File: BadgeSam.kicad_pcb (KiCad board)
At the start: 2 copper layers, 69.6 x 45 mm, 16 parts, among them J1 PROG, SW1 RESET, U1 STM8S003F3P

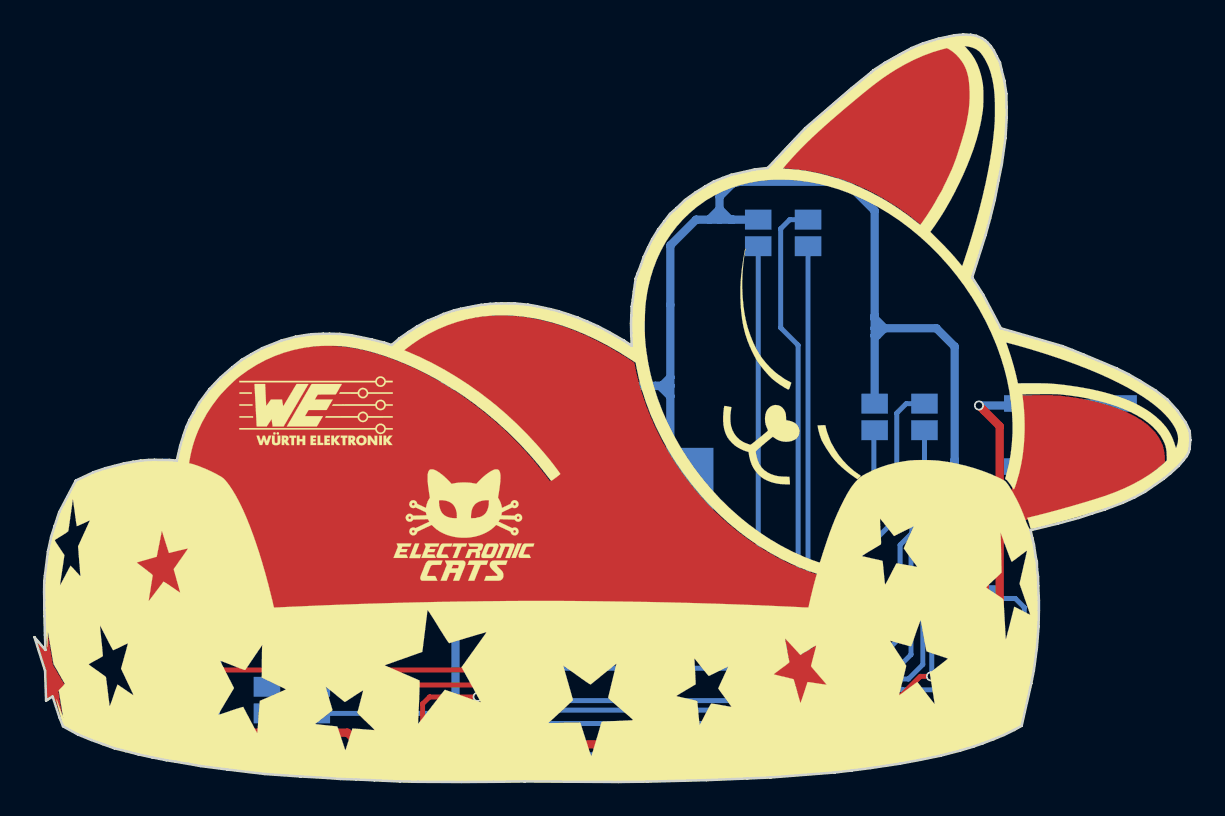
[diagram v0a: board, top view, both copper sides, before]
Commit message: Fix leds and traces
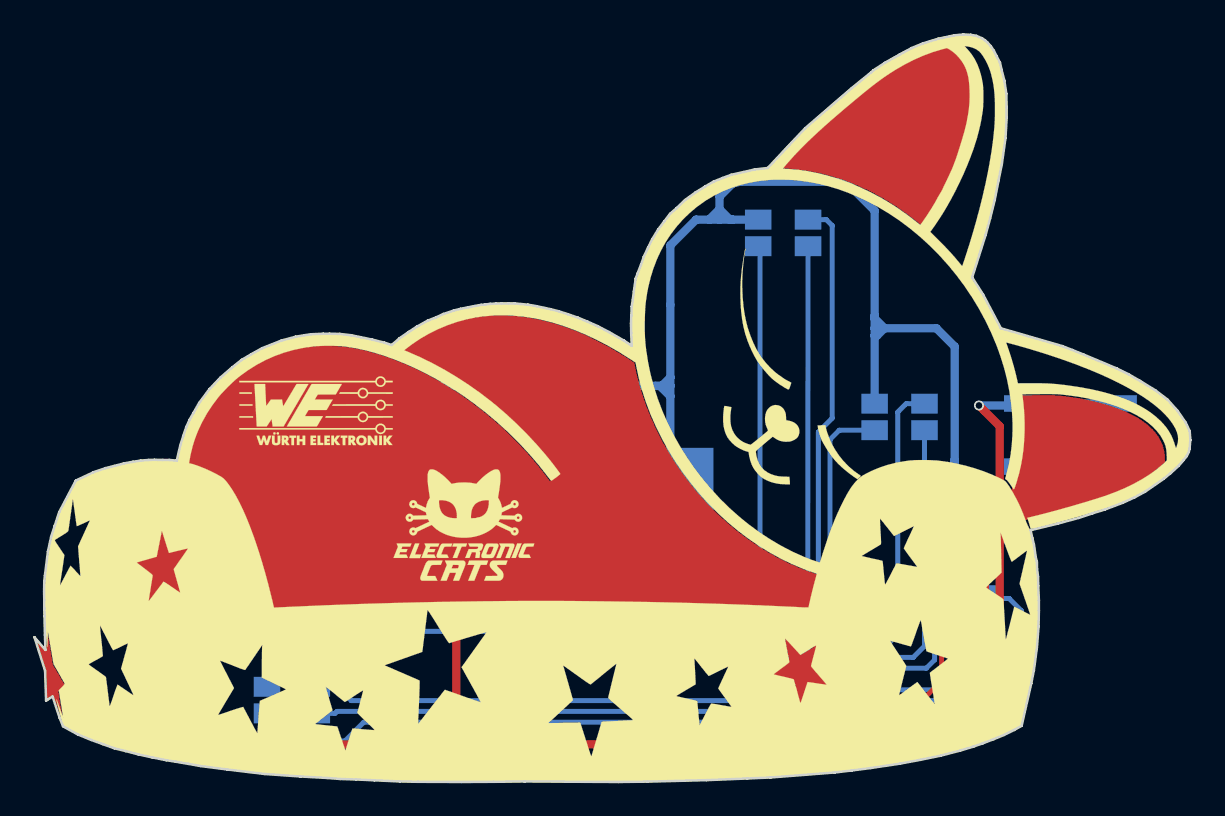
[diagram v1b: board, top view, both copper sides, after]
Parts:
- moved C2 0.42 mm to (167.6, 132.1), turned to 15 degrees
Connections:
- U1 pad 1: /G4 -> /B4
- U1 pad 10: /R1 -> Net-(U1-Pad10)
- U1 pad 11: /B2 -> Net-(U1-Pad11)
- U1 pad 12: /G2 -> Net-(U1-Pad12)
- U1 pad 13: Net-(U1-Pad13) -> /R2
- U1 pad 14: /G3 -> /G2
- U1 pad 15: /R2 -> /B2
- U1 pad 16: Net-(U1-Pad16) -> /R4
- U1 pad 17: Net-(U1-Pad17) -> /B3
- U1 pad 19: /B3 -> /G3
- U1 pad 2: /B4 -> /G4
- U1 pad 3: /R4 -> /B1
- U1 pad 5: /G1 -> /R1
- U1 pad 6: /B1 -> /G1
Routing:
- net GND: track 114.5 -> 102.9 mm, vias 5 -> 6
- net /R1: track 15.4 -> 9.99 mm, vias 2 -> 0
- net /B2: track 31.1 -> 27.0 mm, vias 2 -> 0
- net /G3: track 30.3 -> 27.3 mm
- net /R2: track 34.4 -> 31.5 mm, vias 2 -> 0
- net /RST: track 73.3 -> 76.1 mm, vias 2 -> 3
- net /B3: track 29.7 -> 32.3 mm
- net /B4: track 19.4 -> 17.9 mm
- net +BATT: track 143.2 -> 141.8 mm, vias 5 -> 3
- net /G4: track 15.8 -> 17.3 mm
- net Net-(C1-Pad1): track 9.81 -> 11.1 mm
- net /B1: track 11.0 -> 9.72 mm, vias 2 -> 0
- net /R4: track 21.0 -> 21.7 mm, vias 2 -> 0
- net /SWIM: track 37.6 -> 36.9 mm
- net /G2: track 27.3 -> 26.7 mm, vias 2 -> 0

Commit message: add pcbway logo
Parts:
- added G***: LOGO, Aesthetics:pcbway20x8, F.Cu at (147.6, 120.7)
- moved G*** 28.6 mm to (151.6, 124.7)
- moved G*** 7.39 mm to (132.1, 119.1)
